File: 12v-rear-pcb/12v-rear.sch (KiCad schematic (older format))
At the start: 11 parts

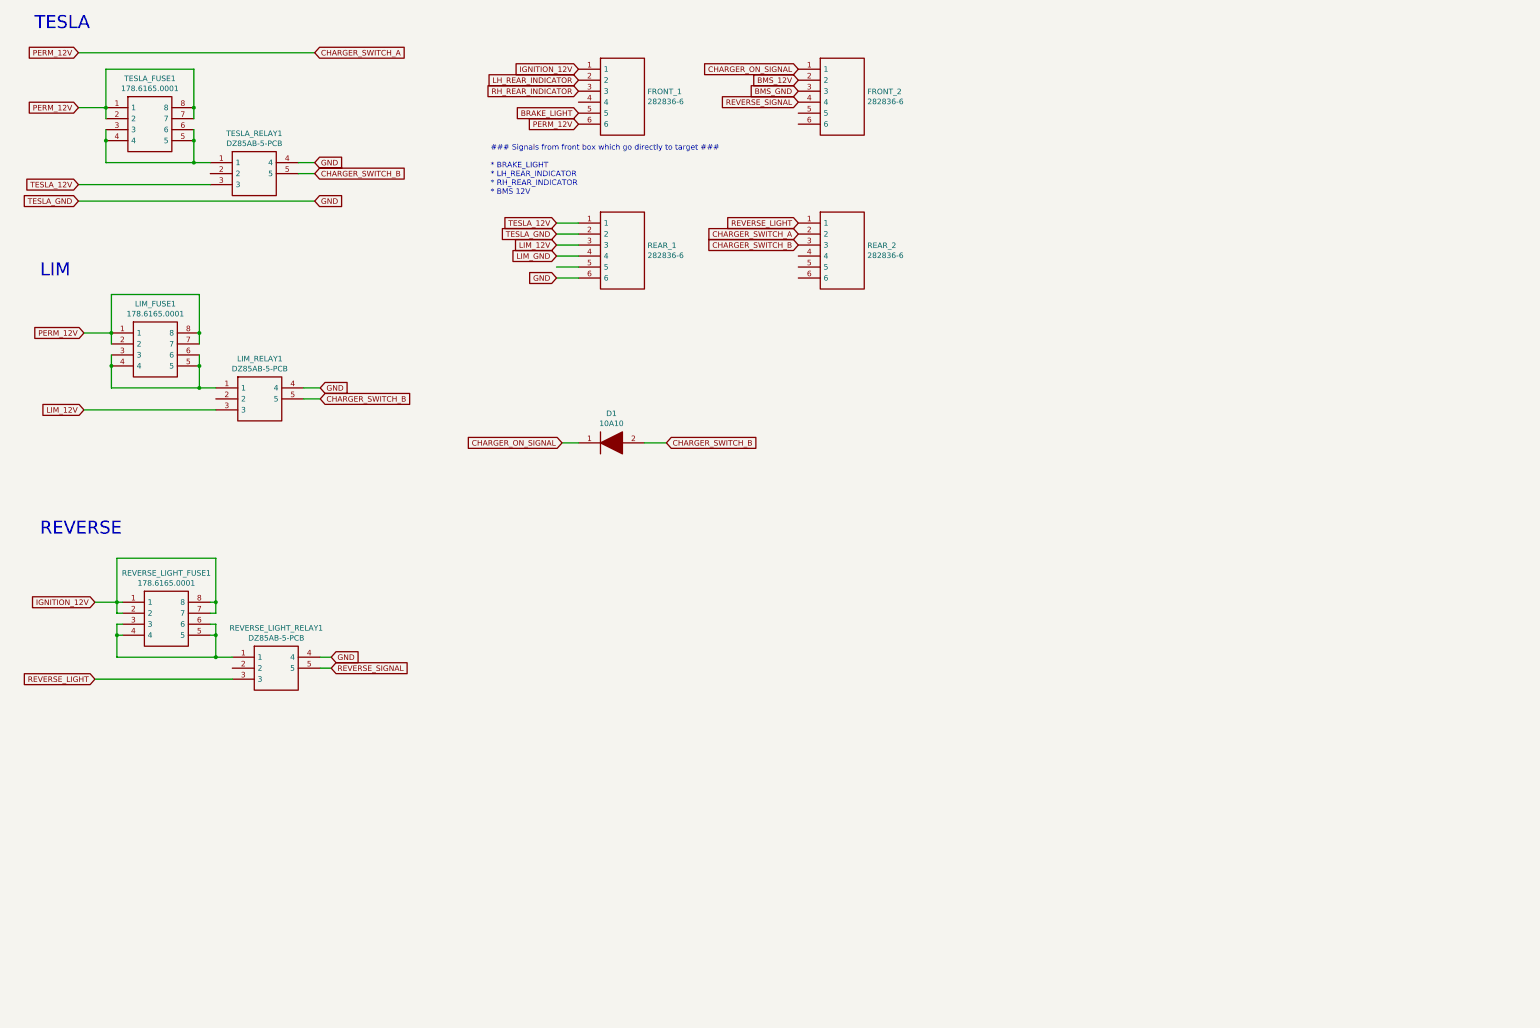
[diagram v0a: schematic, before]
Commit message: Add dash vcu
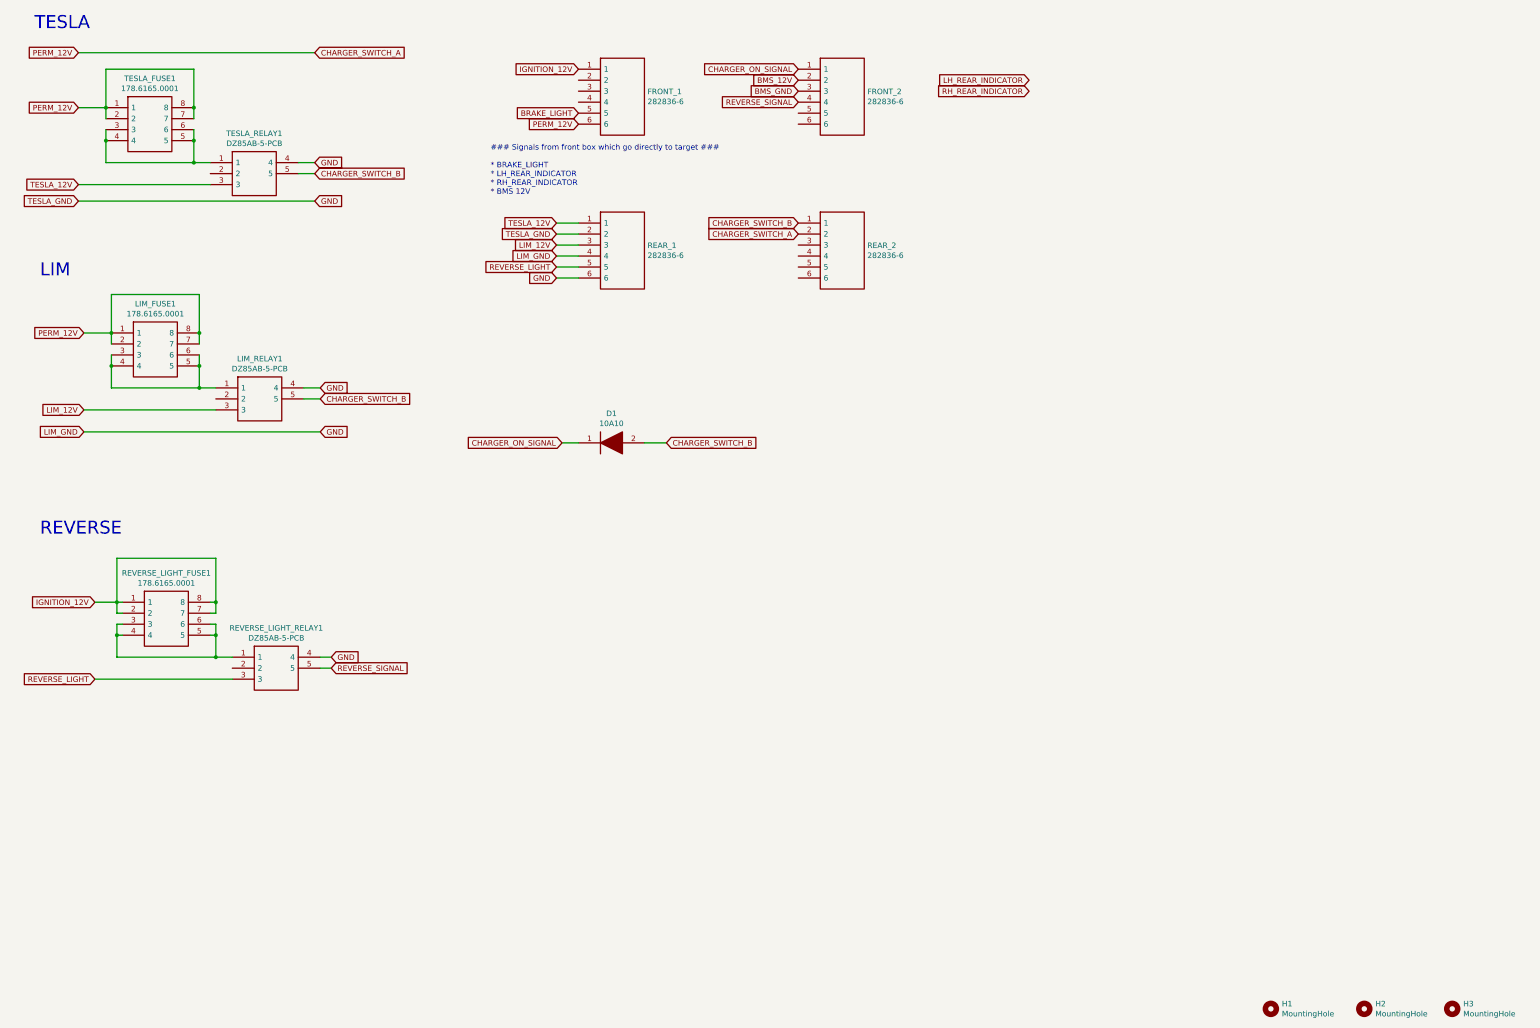
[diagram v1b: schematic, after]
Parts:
- added H1, H2, H3: MountingHole, MountingHole:MountingHole_3mm, symbol Mechanical:MountingHole
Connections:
- net LIM_GND is gone; now on net GND: REAR_1.4
- net CHARGER_SWITCH_B: now also REAR_2.1; no longer REAR_2.3
- net LH_REAR_INDICATOR: no longer FRONT_1.2
- net REVERSE_LIGHT: now also REAR_1.5; no longer REAR_2.1
- net RH_REAR_INDICATOR: no longer FRONT_1.3
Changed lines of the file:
@@
 Text GLabel 7750 2650 0    50   Input ~ 0
 CHARGER_SWITCH_A
-Text GLabel 7750 2750 0    50   Input ~ 0
+Text GLabel 7750 2550 0    50   Input ~ 0
 CHARGER_SWITCH_B
 Wire Wire Line
@@
 	1    0    0    -1
 $EndComp
-Text GLabel 7750 2550 0    50   Input ~ 0
+Text GLabel 5550 2950 0    50   Input ~ 0
 REVERSE_LIGHT
 Text Notes 4950 2300 0    50   ~ 0
@@
 Text GLabel 7750 1250 0    50   Input ~ 0
 BMS_12V
-Text GLabel 5750 1350 0    50   Input ~ 0
+Text GLabel 9850 1350 0    50   Input ~ 0
 RH_REAR_INDICATOR
 Text GLabel 5750 1550 0    50   Input ~ 0
 BRAKE_LIGHT
-Text GLabel 5750 1250 0    50   Input ~ 0
+Text GLabel 9850 1250 0    50   Input ~ 0
 LH_REAR_INDICATOR
 Text GLabel 5550 2650 0    50   Input ~ 0
@@
 Text Notes 850  5400 0    118  ~ 0
 REVERSE
+Text GLabel 3400 4450 2    50   Input ~ 0
+GND
+Text GLabel 1250 4450 0    50   Input ~ 0
+LIM_GND
+Wire Wire Line
+	3400 4450 1250 4450
+$Comp
+L Mechanical:MountingHole H1
+U 1 1 61AB741D
+P 12050 9700
+F 0 "H1" H 12150 9746 50  0000 L CNN
+F 1 "MountingHole" H 12150 9655 50  0000 L CNN
+F 2 "MountingHole:MountingHole_3mm" H 12050 9700 50  0001 C CNN
+F 3 "~" H 12050 9700 50  0001 C CNN
+	1    12050 9700
+	1    0    0    -1
+$EndComp
+$Comp
+L Mechanical:MountingHole H2
+U 1 1 61AB79CE
+P 12900 9700
+F 0 "H2" H 13000 9746 50  0000 L CNN
+F 1 "MountingHole" H 13000 9655 50  0000 L CNN
+F 2 "MountingHole:MountingHole_3mm" H 12900 9700 50  0001 C CNN
+F 3 "~" H 12900 9700 50  0001 C CNN
+	1    12900 9700
+	1    0    0    -1
+$EndComp
+$Comp
+L Mechanical:MountingHole H3
+U 1 1 61AB7EEF
+P 13700 9700
+F 0 "H3" H 13800 9746 50  0000 L CNN
+F 1 "MountingHole" H 13800 9655 50  0000 L CNN
+F 2 "MountingHole:MountingHole_3mm" H 13700 9700 50  0001 C CNN
+F 3 "~" H 13700 9700 50  0001 C CNN
+	1    13700 9700
+	1    0    0    -1
+$EndComp
 $EndSCHEMATC
